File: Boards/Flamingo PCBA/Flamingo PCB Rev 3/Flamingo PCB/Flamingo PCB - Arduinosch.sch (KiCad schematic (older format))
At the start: 19 parts, among them J201 FTDI_Header, J202 ICSP_Header, U201 ATMEGA328P-AU, Y201 Resonator

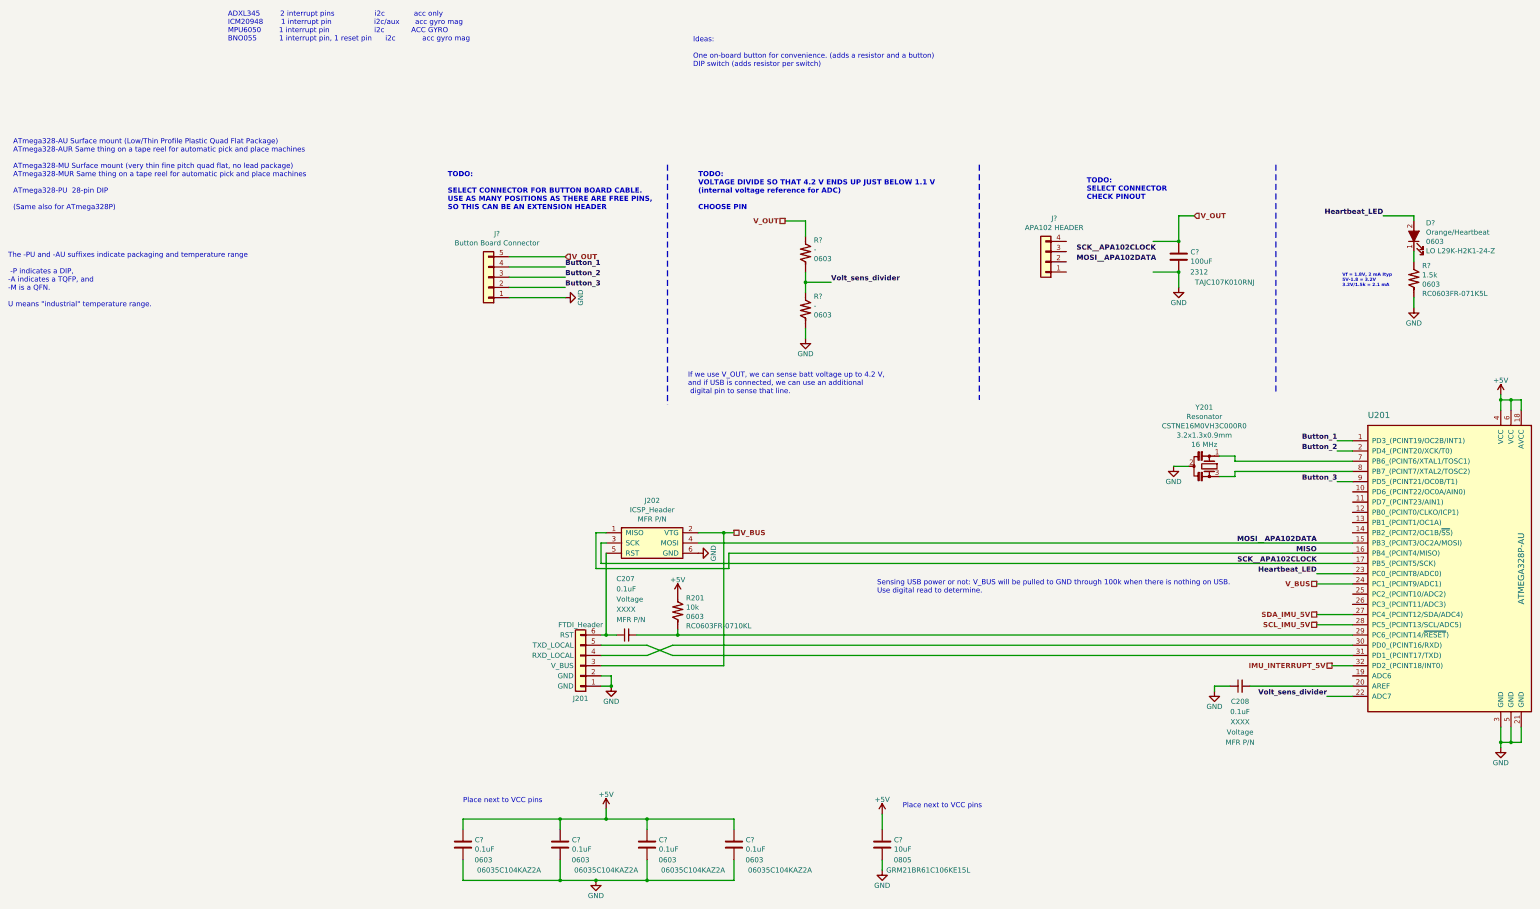
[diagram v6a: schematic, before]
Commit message: Wired up top-level sheet, fixed some hier. pins
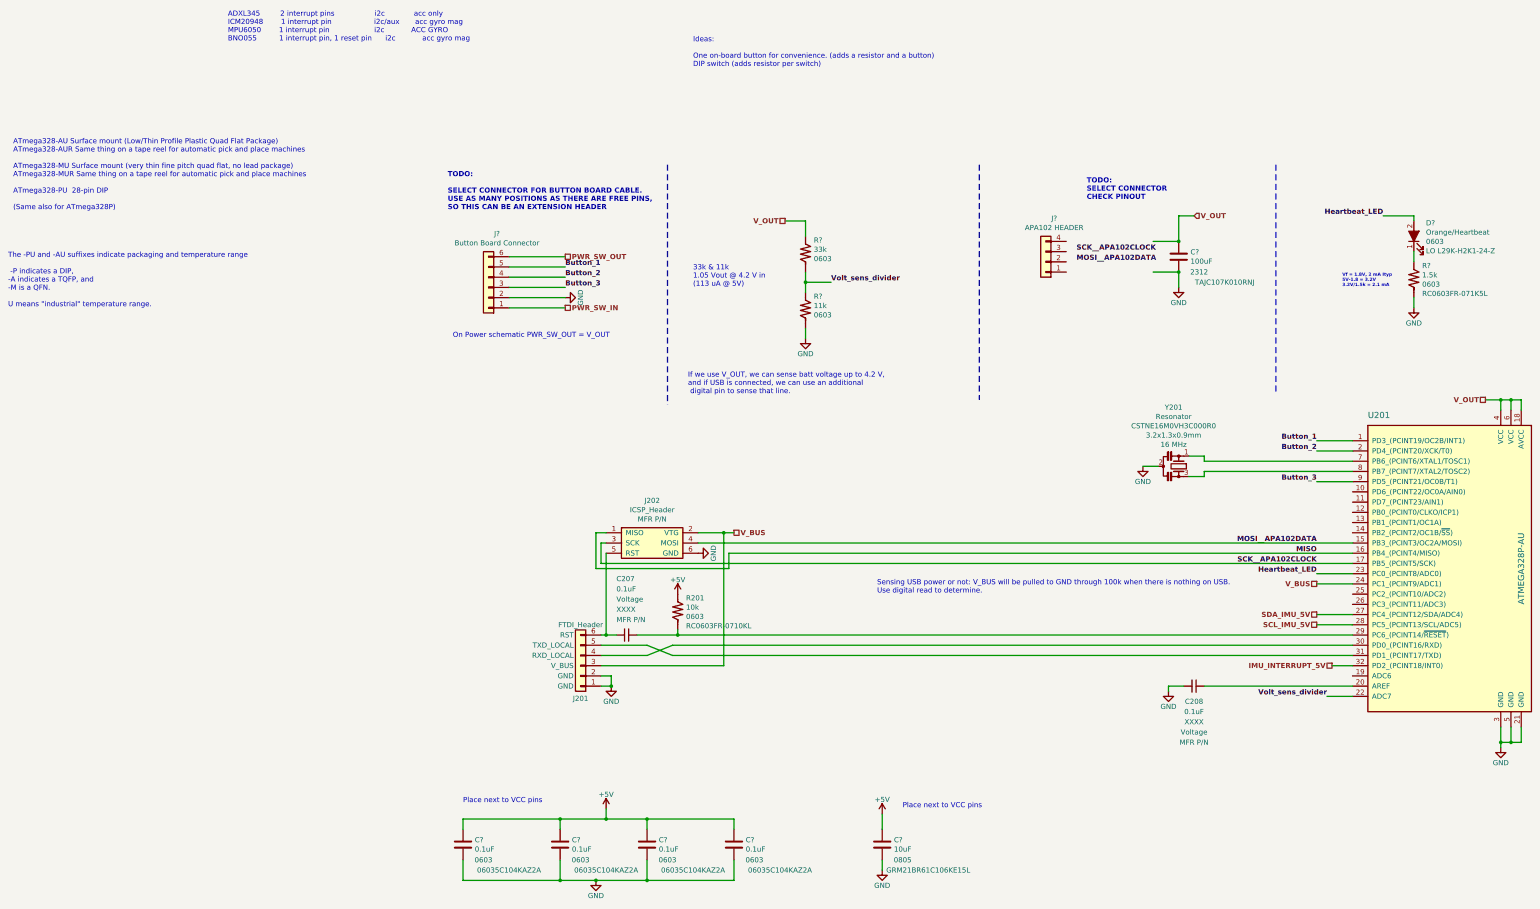
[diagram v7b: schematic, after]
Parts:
- removed J?: Button Board Connector, symbol Connector_Generic:Conn_01x05
- added J?: Button Board Connector, symbol Connector_Generic:Conn_01x06
- R?: value - -> 11k
- R?: value - -> 33k
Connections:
- net +5V: no longer U201.18 (AVCC), U201.4 (VCC), U201.6 (VCC)
- net Button_1: now also J?.5 (Pin_5)
- net Button_2: now also J?.4 (Pin_4)
- net Button_3: now also J?.3 (Pin_3)
- net GND: now also J?.2 (Pin_2)
- net V_OUT: now also U201.18 (AVCC), U201.4 (VCC), U201.6 (VCC)
- new net PWR_SW_IN: J?.1 (Pin_1)
- new net PWR_SW_OUT: J?.6 (Pin_6)
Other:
- note added: "33k & 11k \n1.05 Vout @ 4.2 V in \n(113 uA @ 5V)\n"
- note added: "On Power schematic PWR_SW_OUT = V_OUT"
- note removed: "TODO: \nVOLTAGE DIVIDE SO THAT 4.2 V ENDS UP JUST BELOW 1.1 V \n(internal voltage reference for ADC)\n\nCHOOSE PIN"
- moved on the sheet: C208, Y201
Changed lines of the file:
@@
 $Descr A4 11693 8268
 encoding utf-8
-Sheet 2 5
+Sheet 5 5
 Title ""
 Date ""
@@
 Wire Wire Line
 	2750 5200 2500 5300
-$Comp
-L power:+5V #PWR0206
-U 1 1 5F869CB1
-P 10850 2750
-F 0 "#PWR0206" H 10850 2600 50  0001 C CNN
-F 1 "+5V" H 10850 2890 50  0000 C CNN
-F 2 "" H 10850 2750 50  0001 C CNN
-F 3 "" H 10850 2750 50  0001 C CNN
-	1    10850 2750
-	1    0    0    -1
-$EndComp
-Wire Wire Line
-	10850 2750 10850 2800
 Wire Wire Line
 	10950 2900 10950 2800
 Wire Wire Line
 	10950 2800 10850 2800
-Connection ~ 10850 2800
 Wire Wire Line
 	10850 2800 10850 2900
@@
 L power:GND #PWR0204
 U 1 1 5F8980D8
-P 7650 3450
-F 0 "#PWR0204" H 7650 3200 50  0001 C CNN
-F 1 "GND" H 7650 3300 50  0000 C CNN
-F 2 "" H 7650 3450 50  0001 C CNN
-F 3 "" H 7650 3450 50  0001 C CNN
-	1    7650 3450
-	1    0    0    -1
-$EndComp
-Wire Wire Line
-	7650 3450 7800 3450
+P 7350 3450
+F 0 "#PWR0204" H 7350 3200 50  0001 C CNN
+F 1 "GND" H 7350 3300 50  0000 C CNN
+F 2 "" H 7350 3450 50  0001 C CNN
+F 3 "" H 7350 3450 50  0001 C CNN
+	1    7350 3450
+	1    0    0    -1
+$EndComp
+Wire Wire Line
+	7350 3450 7500 3450
 $Comp
 L MyCrystals:Resonator_Small_vert Y201
 U 1 1 5F8A8BD5
-P 8000 3450
-F 0 "Y201" V 7423 3400 50  0000 C CNN
-F 1 "Resonator" V 7514 3400 50  0000 C CNN
-F 2 "" H 7975 3450 50  0001 C CNN
-F 3 "https://www.murata.com/en/products/productdata/8801162264606/SPEC-CSTNE16M0VH3C000R0.pdf" H 7975 3450 50  0001 C CNN
-F 4 "CSTNE16M0VH3C000R0" V 7605 3400 50  0000 C CNN "MPN"
-F 5 "490-17951-1-ND" H 8000 3450 50  0001 C CNN "Digi-Key_PN"
-F 6 "Y" H 8000 3450 50  0001 C CNN "Prefix"
-F 7 "https://www.digikey.com/en/products/detail/murata-electronics/CSTNE16M0VH3C000R0/8747732" H 8000 3450 50  0001 C CNN "Website"
-F 8 "CERAMIC RES 16.0000MHZ 15PF SMD" H 8000 3450 50  0001 C CNN "Description"
-F 9 "Murata Electronics" H 8000 3450 50  0001 C CNN "Manufacturer"
-F 10 "3.2x1.3x0.9mm" V 7696 3400 50  0000 C CNN "Package"
-F 11 "16 MHz" V 7787 3400 50  0000 C CNN "Frequency"
-	1    8000 3450
+P 7700 3450
+F 0 "Y201" V 7123 3400 50  0000 C CNN
+F 1 "Resonator" V 7214 3400 50  0000 C CNN
+F 2 "" H 7675 3450 50  0001 C CNN
+F 3 "https://www.murata.com/en/products/productdata/8801162264606/SPEC-CSTNE16M0VH3C000R0.pdf" H 7675 3450 50  0001 C CNN
+F 4 "CSTNE16M0VH3C000R0" V 7305 3400 50  0000 C CNN "MPN"
+F 5 "490-17951-1-ND" H 7700 3450 50  0001 C CNN "Digi-Key_PN"
+F 6 "Y" H 7700 3450 50  0001 C CNN "Prefix"
+F 7 "https://www.digikey.com/en/products/detail/murata-electronics/CSTNE16M0VH3C000R0/8747732" H 7700 3450 50  0001 C CNN "Website"
+F 8 "CERAMIC RES 16.0000MHZ 15PF SMD" H 7700 3450 50  0001 C CNN "Description"
+F 9 "Murata Electronics" H 7700 3450 50  0001 C CNN "Manufacturer"
+F 10 "3.2x1.3x0.9mm" V 7396 3400 50  0000 C CNN "Package"
+F 11 "16 MHz" V 7487 3400 50  0000 C CNN "Frequency"
+	1    7700 3450
 	0    1    1    0
 $EndComp
@@
 L MyCapacitors:C_Small_horizontal C208
 U 1 1 5F8AF43A
-P 8400 5550
-F 0 "C208" H 8300 5350 50  0000 C CNN
-F 1 "0.1uF" H 8300 5250 50  0000 C CNN
-F 2 "" V 8275 5500 50  0001 L CNN
-F 3 "" H 8200 6025 50  0001 L CNN
-F 4 "XXXX" H 8300 5150 50  0000 C CNN "Package Size"
-F 5 "Voltage" H 8300 5050 50  0000 C CNN "Voltage Rating"
-F 6 "MFR P/N" H 8300 4950 50  0000 C CNN "MPN"
-F 7 "-" H 8200 5850 50  0001 L CNN "Digi-Key_PN"
-F 8 "C" H 8200 5850 50  0001 L CNN "Prefix"
-F 9 "-" H 8200 5850 50  0001 L CNN "Website"
-F 10 "-" H 8200 5850 50  0001 L CNN "Description"
-F 11 "-" H 8200 5850 50  0001 L CNN "Manufacturer"
-	1    8400 5550
+P 7950 5550
+F 0 "C208" H 7850 5350 50  0000 C CNN
+F 1 "0.1uF" H 7850 5250 50  0000 C CNN
+F 2 "" V 7825 5500 50  0001 L CNN
+F 3 "" H 7750 6025 50  0001 L CNN
+F 4 "XXXX" H 7850 5150 50  0000 C CNN "Package Size"
+F 5 "Voltage" H 7850 5050 50  0000 C CNN "Voltage Rating"
+F 6 "MFR P/N" H 7850 4950 50  0000 C CNN "MPN"
+F 7 "-" H 7750 5850 50  0001 L CNN "Digi-Key_PN"
+F 8 "C" H 7750 5850 50  0001 L CNN "Prefix"
+F 9 "-" H 7750 5850 50  0001 L CNN "Website"
+F 10 "-" H 7750 5850 50  0001 L CNN "Description"
+F 11 "-" H 7750 5850 50  0001 L CNN "Manufacturer"
+	1    7950 5550
 	1    0    0    -1
 $EndComp
@@
 L power:GND #PWR0205
 U 1 1 5F8B38E2
-P 8050 5650
-F 0 "#PWR0205" H 8050 5400 50  0001 C CNN
-F 1 "GND" H 8050 5500 50  0000 C CNN
-F 2 "" H 8050 5650 50  0001 C CNN
-F 3 "" H 8050 5650 50  0001 C CNN
-	1    8050 5650
-	1    0    0    -1
-$EndComp
-Wire Wire Line
-	8050 5600 8050 5650
-Wire Wire Line
-	8050 5600 8200 5600
+P 7600 5650
+F 0 "#PWR0205" H 7600 5400 50  0001 C CNN
+F 1 "GND" H 7600 5500 50  0000 C CNN
+F 2 "" H 7600 5650 50  0001 C CNN
+F 3 "" H 7600 5650 50  0001 C CNN
+	1    7600 5650
+	1    0    0    -1
+$EndComp
+Wire Wire Line
+	7600 5600 7600 5650
+Wire Wire Line
+	7600 5600 7750 5600
 Wire Wire Line
 	2800 5050 2800 5100
@@
 MISO
 Wire Wire Line
-	9250 3200 9400 3200
-Wire Wire Line
-	9250 3300 9400 3300
-Wire Wire Line
-	8100 3350 8250 3350
-Wire Wire Line
-	8250 3350 8250 3400
-Wire Wire Line
-	8250 3400 9400 3400
-Wire Wire Line
-	8100 3550 8250 3550
-Wire Wire Line
-	8250 3550 8250 3500
-Wire Wire Line
-	8250 3500 9400 3500
+	9050 3200 9400 3200
+Wire Wire Line
+	9050 3300 9400 3300
+Wire Wire Line
+	7800 3350 7950 3350
+Wire Wire Line
+	7950 3350 7950 3400
+Wire Wire Line
+	7800 3550 7950 3550
+Wire Wire Line
+	7950 3550 7950 3500
 Text Label 9050 4400 2    50   ~ 10
 SCK__APA102CLOCK
@@
 Heartbeat_LED
 Wire Wire Line
-	9250 3600 9400 3600
+	9050 3600 9400 3600
 Text Notes -1600 -700 0    50   ~ 0
 ADXL345         2 interrupt pins                  i2c             acc only\nICM20948        1 interrupt pin                   i2c/aux       acc gyro mag\nMPU6050        1 interrupt pin                    i2c            ACC GYRO\nBNO055          1 interrupt pin, 1 reset pin      i2c            acc gyro mag\n
@@
 Text Notes 5000 6800 0    50   ~ 0
 Place next to VCC pins
-Text Label 9250 3200 2    50   ~ 10
+Text Label 9050 3200 2    50   ~ 10
 Button_1
-Text Label 9250 3300 2    50   ~ 10
+Text Label 9050 3300 2    50   ~ 10
 Button_2
-Text Label 9250 3600 2    50   ~ 10
+Text Label 9050 3600 2    50   ~ 10
 Button_3
 Text Notes 2950 -450 0    50   ~ 0
@@
 Text Label 1700 1700 0    50   ~ 10
 Button_3
-Text HLabel 1700 1400 2    50   Input ~ 10
-V_OUT
 $Comp
 L power:GND #PWR?
@@
 	0    -1   -1   0
 $EndComp
-$Comp
-L Connector_Generic:Conn_01x05 J?
-U 1 1 5F87A6A8
-P 950 1600
-F 0 "J?" H 868 1175 50  0000 C CNN
-F 1 "Button Board Connector" H 868 1266 50  0000 C CNN
-F 2 "" H 950 1600 50  0001 C CNN
-F 3 "~" H 950 1600 50  0001 C CNN
-	1    950  1600
-	-1   0    0    1
-$EndComp
 Wire Wire Line
 	1150 1400 1700 1400
@@
 Wire Wire Line
 	1150 1600 1700 1600
-Wire Wire Line
-	8400 5600 9400 5600
 Wire Wire Line
 	9150 5700 9400 5700
@@
 Text Notes 2900 2750 0    50   ~ 0
 If we use V_OUT, we can sense batt voltage up to 4.2 V, \nand if USB is connected, we can use an additional\n digital pin to sense that line.
-Text Notes 3000 950  0    50   ~ 10
-TODO: \nVOLTAGE DIVIDE SO THAT 4.2 V ENDS UP JUST BELOW 1.1 V \n(internal voltage reference for ADC)\n\nCHOOSE PIN
 Wire Wire Line
 	4050 1650 4050 1750
@@
 AR Path="/5F780A01/5FA738C9" Ref="R?"  Part="1"
 F 0 "R?" H 4131 1462 50  0000 L CNN
-F 1 "-" H 4131 1371 50  0000 L CNN
+F 1 "33k" H 4131 1371 50  0000 L CNN
 F 2 "Resistors_SMD:R_0603_HandSoldering" V 4105 1300 50  0001 C CNN
 F 3 "" H 4050 1350 50  0001 C CNN
@@
 AR Path="/5F780A01/5FA70FC9" Ref="R?"  Part="1"
 F 0 "R?" H 4131 2012 50  0000 L CNN
-F 1 "-" H 4131 1921 50  0000 L CNN
+F 1 "11k" H 4131 1921 50  0000 L CNN
 F 2 "Resistors_SMD:R_0603_HandSoldering" V 4105 1850 50  0001 C CNN
 F 3 "" H 4050 1900 50  0001 C CNN
@@
 Wire Notes Line
 	8650 500  8650 2750
+Text HLabel 1700 1900 2    50   UnSpc ~ 10
+PWR_SW_IN
+Text HLabel 1700 1400 2    50   UnSpc ~ 10
+PWR_SW_OUT
+$Comp
+L Connector_Generic:Conn_01x06 J?
+U 1 1 5F88EBD8
+P 950 1700
+F 0 "J?" H 868 1175 50  0000 C CNN
+F 1 "Button Board Connector" H 868 1266 50  0000 C CNN
+F 2 "" H 950 1700 50  0001 C CNN
+F 3 "~" H 950 1700 50  0001 C CNN
+	1    950  1700
+	-1   0    0    1
+$EndComp
+Wire Wire Line
+	1700 1900 1150 1900
+Text Notes 600  2200 0    50   ~ 0
+On Power schematic PWR_SW_OUT = V_OUT
+Text Notes 2950 1700 0    50   ~ 0
+33k & 11k  \n1.05 Vout @ 4.2 V in \n(113 uA @ 5V)\n
+Wire Wire Line
+	7950 3400 9400 3400
+Wire Wire Line
+	7950 3500 9400 3500
+Wire Wire Line
+	7950 5600 9400 5600
+Text HLabel 10700 2800 0    50   UnSpc ~ 10
+V_OUT
+Wire Wire Line
+	10700 2800 10850 2800
+Connection ~ 10850 2800
 $EndSCHEMATC

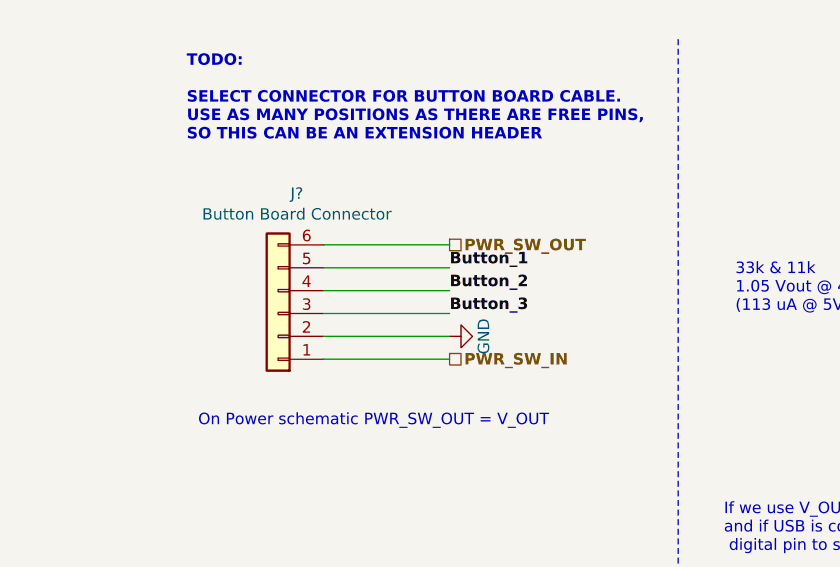
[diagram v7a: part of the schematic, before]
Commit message: Added Button Remote project
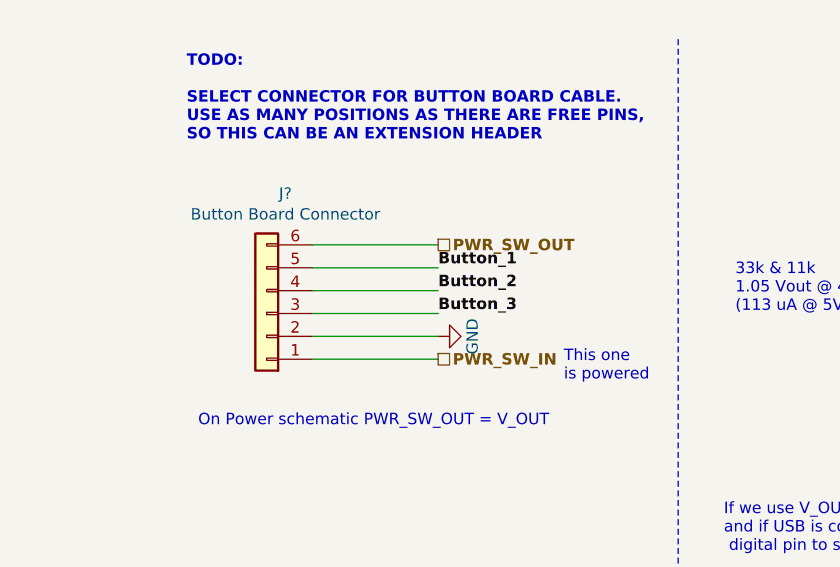
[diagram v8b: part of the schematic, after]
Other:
- note added: "This one \nis powered"
- moved on the sheet: J?
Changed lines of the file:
@@
 $Descr A4 11693 8268
 encoding utf-8
-Sheet 5 5
+Sheet 4 4
 Title ""
 Date ""
@@
 Text Notes 2950 -450 0    50   ~ 0
 Ideas:\n\nOne on-board button for convenience. (adds a resistor and a button)\nDIP switch (adds resistor per switch)
-Text Label 1700 1500 0    50   ~ 10
+Text Label 1650 1500 0    50   ~ 10
 Button_1
-Text Label 1700 1600 0    50   ~ 10
+Text Label 1650 1600 0    50   ~ 10
 Button_2
-Text Label 1700 1700 0    50   ~ 10
+Text Label 1650 1700 0    50   ~ 10
 Button_3
 $Comp
 L power:GND #PWR?
 U 1 1 5F875030
-P 1700 1800
-F 0 "#PWR?" H 1700 1550 50  0001 C CNN
-F 1 "GND" H 1700 1650 50  0000 C CNN
-F 2 "" H 1700 1800 50  0001 C CNN
-F 3 "" H 1700 1800 50  0001 C CNN
-	1    1700 1800
+P 1650 1800
+F 0 "#PWR?" H 1650 1550 50  0001 C CNN
+F 1 "GND" H 1650 1650 50  0000 C CNN
+F 2 "" H 1650 1800 50  0001 C CNN
+F 3 "" H 1650 1800 50  0001 C CNN
+	1    1650 1800
 	0    -1   -1   0
 $EndComp
 Wire Wire Line
-	1150 1400 1700 1400
-Wire Wire Line
-	1150 1500 1700 1500
-Wire Wire Line
-	1150 1800 1700 1800
-Wire Wire Line
-	1150 1700 1700 1700
-Wire Wire Line
-	1150 1600 1700 1600
+	1100 1400 1650 1400
+Wire Wire Line
+	1100 1500 1650 1500
+Wire Wire Line
+	1100 1800 1650 1800
+Wire Wire Line
+	1100 1700 1650 1700
+Wire Wire Line
+	1100 1600 1650 1600
 Wire Wire Line
 	9150 5700 9400 5700
@@
 Wire Notes Line
 	8650 500  8650 2750
-Text HLabel 1700 1900 2    50   UnSpc ~ 10
+Text HLabel 1650 1900 2    50   UnSpc ~ 10
 PWR_SW_IN
-Text HLabel 1700 1400 2    50   UnSpc ~ 10
+Text HLabel 1650 1400 2    50   UnSpc ~ 10
 PWR_SW_OUT
 $Comp
 L Connector_Generic:Conn_01x06 J?
 U 1 1 5F88EBD8
-P 950 1700
-F 0 "J?" H 868 1175 50  0000 C CNN
-F 1 "Button Board Connector" H 868 1266 50  0000 C CNN
-F 2 "" H 950 1700 50  0001 C CNN
-F 3 "~" H 950 1700 50  0001 C CNN
-	1    950  1700
+P 900 1700
+F 0 "J?" H 818 1175 50  0000 C CNN
+F 1 "Button Board Connector" H 818 1266 50  0000 C CNN
+F 2 "" H 900 1700 50  0001 C CNN
+F 3 "~" H 900 1700 50  0001 C CNN
+	1    900  1700
 	-1   0    0    1
 $EndComp
 Wire Wire Line
-	1700 1900 1150 1900
+	1650 1900 1100 1900
 Text Notes 600  2200 0    50   ~ 0
 On Power schematic PWR_SW_OUT = V_OUT
@@
 	10700 2800 10850 2800
 Connection ~ 10850 2800
+Text Notes 2200 2000 0    50   ~ 0
+This one \nis powered
 $EndSCHEMATC
